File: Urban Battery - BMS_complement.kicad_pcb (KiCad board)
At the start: 2 copper layers, 149.9 x 83.8 mm, 43 parts, among them J1 BMS IO, J10 Thermistor, J11 Thermistor, J12 CAN Connector, J13 CAN Connector, J14 E-Stop, J2 OLED Header, J3 E-Stop, J4 E-Stop, J5 E-Stop, J6 Contactor Connector, J7 Charge Connector, J8 Battery Connector, J9 Thermistor, K1 Contactor_Relay, K2 Charge_Relay, SW1 SW_SPST, SW2 SW_DPDT_x2, SW3 CAN_TERM, U1 MCP2515-xSO, U2 LM2575HVS-12/NOPB, U3 MCP2551-I-SN, Y1 8MHz

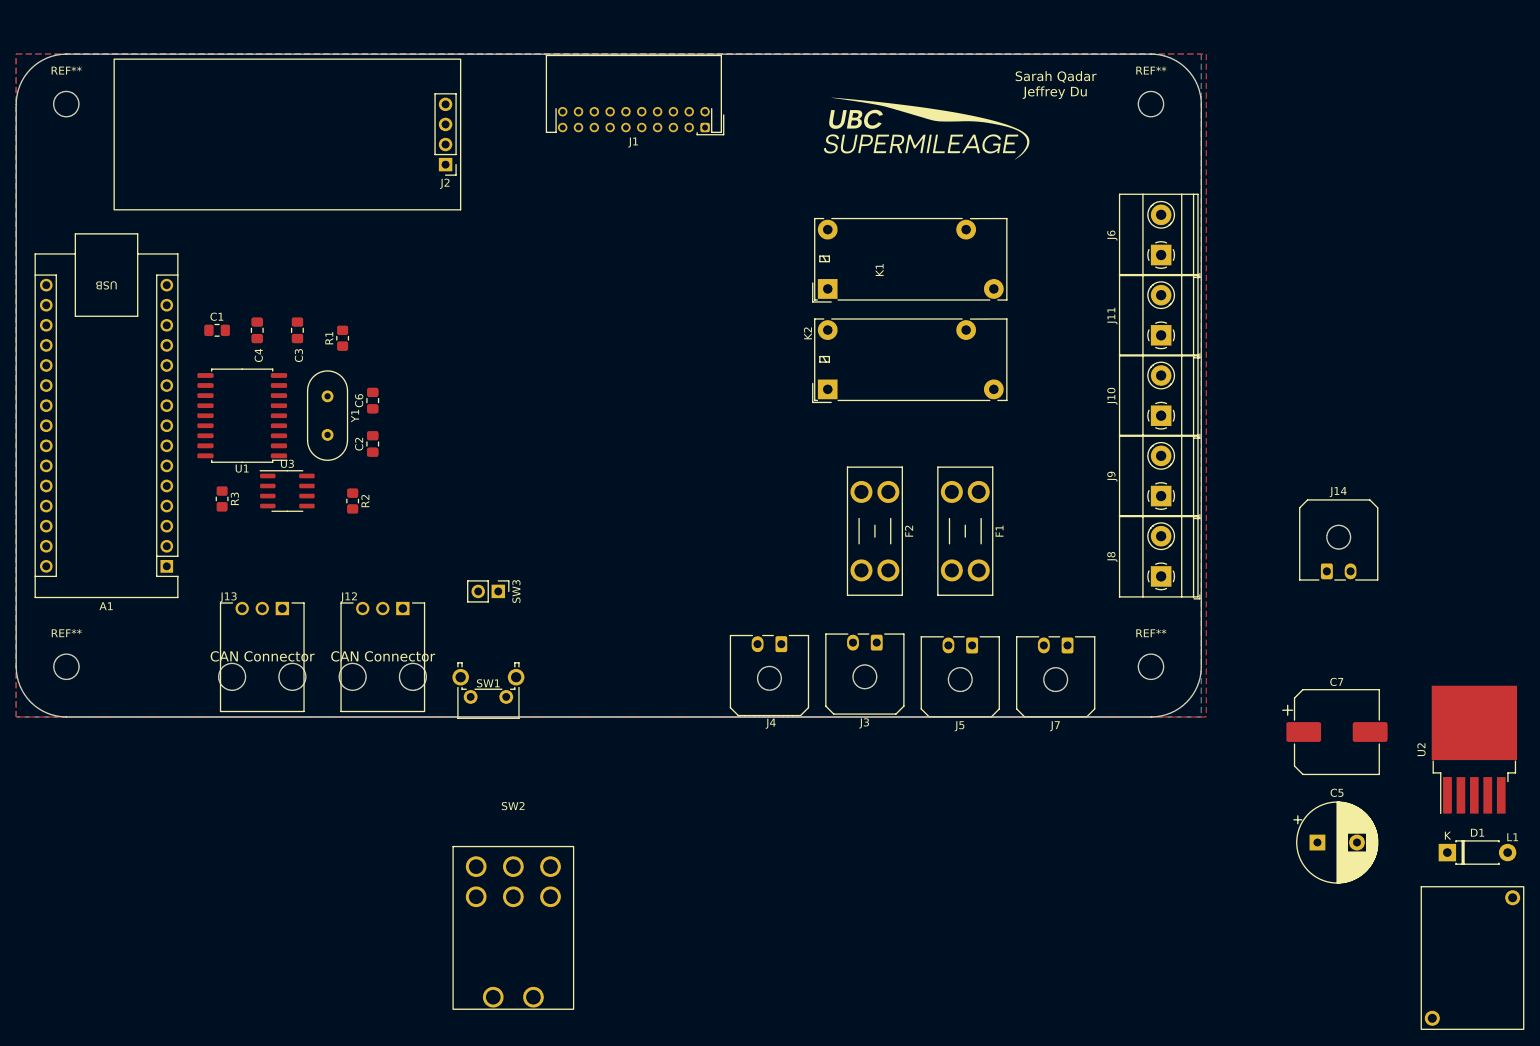
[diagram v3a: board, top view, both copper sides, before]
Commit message: First layout complete
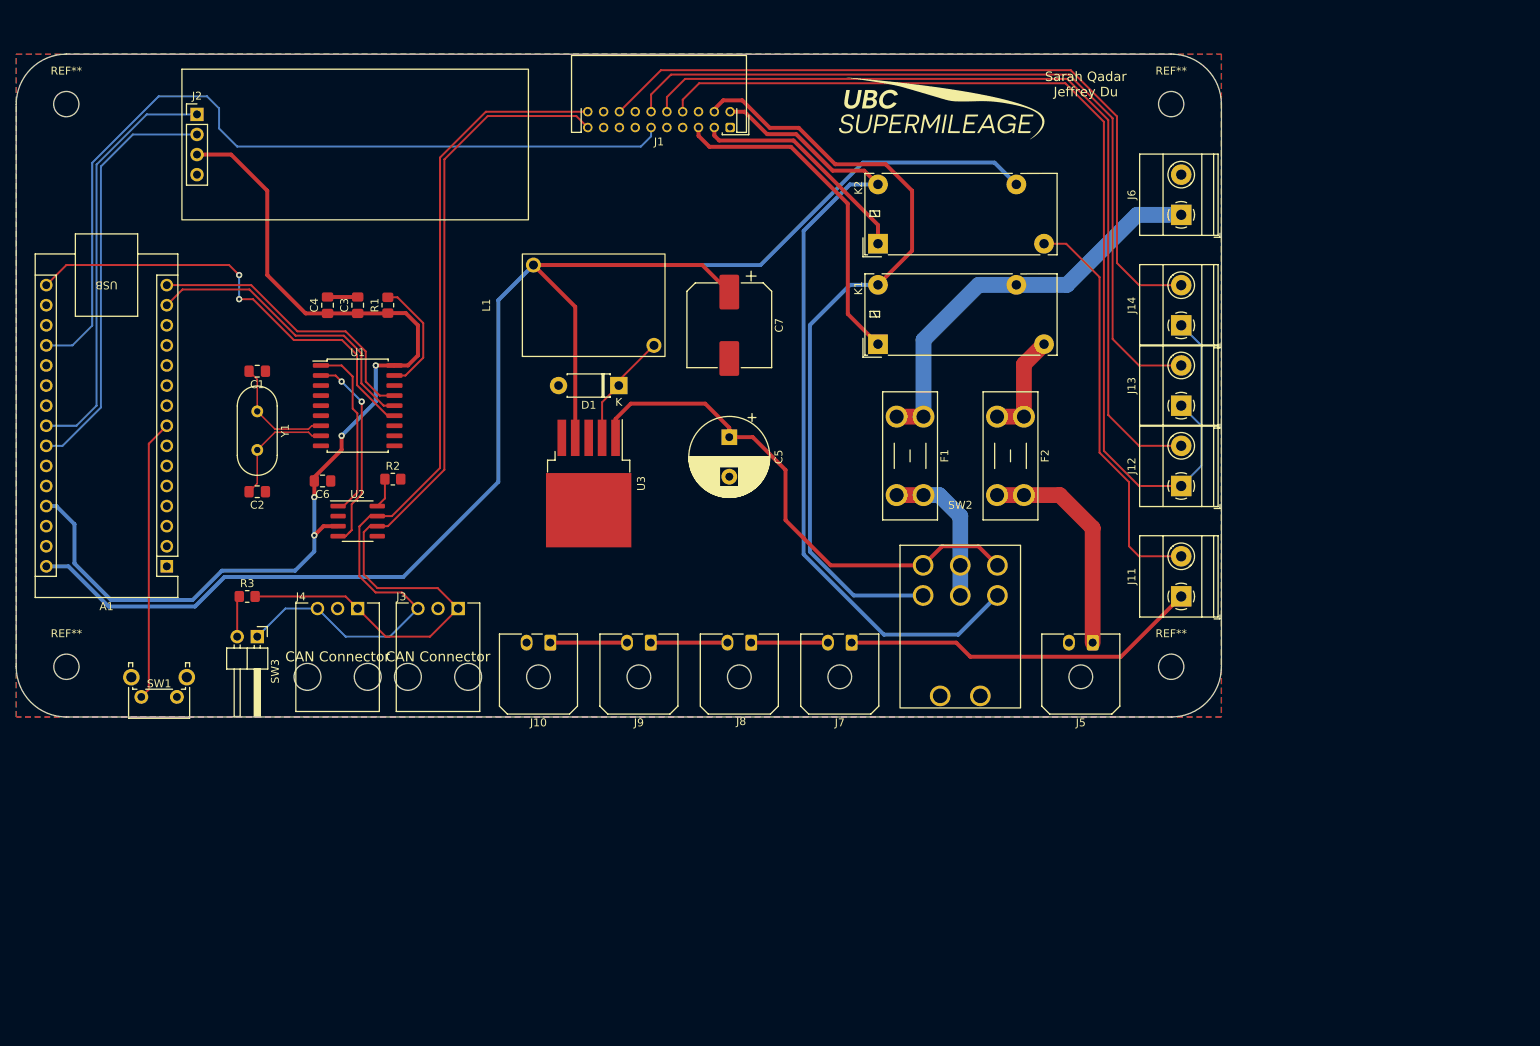
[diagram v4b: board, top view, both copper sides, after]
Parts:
- SW3: footprint Connector_PinHeader_2.54mm:PinHeader_1x02_P2.54mm_Vertical -> Connector_PinHeader_2.54mm:PinHeader_1x02_P2.54mm_Horizontal
- moved L1 138.8 mm to (148.6, 82.5), turned to 90 degrees
- moved D1 120.3 mm to (152.4, 92.7), turned to 180 degrees
- moved U3 116.9 mm to (148.6, 105.1), turned to -90 degrees
- moved C7 92.5 mm to (166.4, 85.1), turned to -90 degrees
- moved C5 90.3 mm to (166.4, 99.2), turned to -90 degrees
- moved J9 86.0 mm to (156.4, 125.2), turned to 180 degrees
- moved SW2 68.2 mm to (195.6, 115.4)
- moved J10 53.3 mm to (143.7, 125.2)
- moved J6 45.8 mm to (223.5, 71.1)
- moved J11 43.3 mm to (223.5, 119.4)
- moved SW1 41.6 mm to (96.5, 132.1)
- moved J2 32.1 mm to (99.1, 58.4), turned to 0 degrees
- moved SW3 31.0 mm to (106.7, 124.5)
- moved F2 19.6 mm to (203.6, 96.6)
- moved C2 15.8 mm to (106.7, 106.1), turned to 180 degrees
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- renumbered J5 to J10, J6 to J11, J9 to J12, J10 to J13, J11 to J14, J12 to J3, J13 to J4, J7 to J5, J8 to J6, J3 to J7, J4 to J8, J14 to J9, K2 to K1, K1 to K2, U3 to U2, U2 to U3
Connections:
- net Net-(F1-Pad2) renamed 48V_In
- net Net-(F2-Pad1) renamed Charge_In
- net Net-(F2-Pad2) renamed Charge
- A1 pad 12: CAN_INT -> unconnected-(A1-Pad12)
- A1 pad 13: CAN_CS -> unconnected-(A1-Pad13)
- J11 pad 1: Net-(J6-Pad1) -> Net-(J7-Pad1)
- J11 pad 2: Net-(J3-Pad1) -> Net-(J11-Pad2)
- J12 pad 1: bms10 -> bms8
- J12 pad 2: bms8 -> bms10
- J13 pad 1: bms12 -> bms8
- J13 pad 2: bms8 -> bms12
- J14 pad 1: bms16 -> bms8
- J14 pad 2: bms8 -> bms16
- J7 pad 1: Net-(J3-Pad1) -> Net-(J7-Pad1)
- K2 pad 3: Net-(J6-Pad1) -> Net-(J11-Pad2)
- SW3 pad 1: Net-(R3-Pad1) -> CANH
- SW3 pad 2: CANH -> Net-(R3-Pad1)
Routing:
- net +12V: track 0.00 -> 212.9 mm
- net bms8: track 0.00 -> 136.9 mm
- net +5V: track 0.00 -> 127.3 mm, vias 0 -> 4
- net CANL: track 0.00 -> 122.0 mm
- net CANH: track 0.00 -> 113.7 mm
- net bms10: track 0.00 -> 108.9 mm
- net bms11: track 0.00 -> 107.4 mm
- net bms2: track 0.00 -> 106.0 mm
- net bms12: track 0.00 -> 101.9 mm
- net bms4: track 0.00 -> 100.2 mm
- net bms16: track 0.00 -> 95.3 mm
- net Buck_VIN: track 0.00 -> 66.4 mm
- net SCK: track 0.00 -> 57.0 mm, vias 0 -> 2
- net Net-(A1-Pad23): track 0.00 -> 53.2 mm
- net Net-(A1-Pad24): track 0.00 -> 53.2 mm
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- added copper zone on F.Cu, net GND
- removed copper zone on F.Cu, net +5V
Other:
- board size 149.9 x 83.8 mm -> 152.4 x 83.8 mm

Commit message: Layout updated
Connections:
- A1 pad 19: bms11 -> unconnected-(A1-Pad19)
- A1 pad 22: unconnected-(A1-Pad22) -> bms11
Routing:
- net bms11: track 107.4 -> 119.2 mm
- net Net-(A1-Pad24): track 53.2 -> 54.9 mm
- net +5V: track 127.3 -> 128.2 mm

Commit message: moved supermileage logo
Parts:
- moved G*** 36.1 mm to (158.8, 69.8)
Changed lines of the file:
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@@
   )
   (footprint "LOGO" (layer "F.Cu")
-    (at 193.04 58.42)
+    (at 158.75 69.85)
     (attr board_only exclude_from_pos_files exclude_from_bom)
     (fp_text reference "G***" (at 0 0) (layer "F.Fab")
@@
   (gr_arc (start 82.55 134.62) (mid 78.059872 132.760128) (end 76.2 128.27) (layer "Edge.Cuts") (width 0.1))
   (gr_line (start 228.6 128.27) (end 228.6 57.15) (layer "Edge.Cuts") (width 0.1))
-  (gr_text "Sarah Qadar\nJeffrey Du" (at 211.455 54.61) (layer "F.SilkS")
+  (gr_text "Sarah Qadar\nJeffrey Du" (at 195.58 58.42) (layer "F.SilkS")
     (effects (font (size 1.2 1.2) (thickness 0.15)))
   )

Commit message: Updated traces
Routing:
- net +48V: track 52.2 -> 107.8 mm
- net Charge: track 28.3 -> 56.6 mm
- net Charge_In: track 13.6 -> 27.2 mm
- net CANH: track 113.7 -> 119.1 mm
- net CANL: track 122.0 -> 126.5 mm
- net GND: track 3.81 -> 0.00 mm
- net +12V: track 212.9 -> 216.6 mm
- net 48V_In: track 19.2 -> 22.6 mm
- net Net-(J11-Pad2): track 51.5 -> 49.0 mm
- net Net-(A1-Pad24): track 54.9 -> 57.3 mm
- net bms16: track 95.3 -> 97.7 mm, vias 0 -> 2
- net MISO: track 36.8 -> 38.8 mm
- net bms5: track 42.8 -> 44.6 mm
- net bms3: track 28.8 -> 30.5 mm
- net bms4: track 100.2 -> 101.9 mm
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
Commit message: Updated traces
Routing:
- net +5V: track 127.9 -> 134.8 mm, vias 4 -> 3
- net MISO: track 38.8 -> 38.2 mm
- net MOSI: track 39.3 -> 38.7 mm
- net SCK: track 58.4 -> 57.7 mm
- net Net-(J11-Pad2): track 49.0 -> 48.4 mm
- net Buck_VIN: track 66.9 -> 66.3 mm
